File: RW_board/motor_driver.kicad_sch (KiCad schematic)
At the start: 0 parts

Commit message: Started working on motor driver schematic, added libraries, added motor cad
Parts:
- added IC1: MCT8315Z0HRRYR, QFN50P600X400X80-33N-D, symbol RW_Imports:MCT8315Z0HRRYR
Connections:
- new net GND: IC1.10 (PGND_1), IC1.14 (PGND_2)
- new net Motor_12V: IC1.8 (VM_1), IC1.9 (VM_2)
- new net Motor_Brake: IC1.31 (BRAKE)
- new net Motor_DIR: IC1.29 (DIR)
- new net Motor_FGOUT: IC1.1 (FGOUT)
- new net Motor_OUTA: IC1.11 (OUTA)
- new net Motor_OUTB: IC1.12 (OUTB)
- new net Motor_OUTC: IC1.13 (OUTC)
- new net Motor_PWM: IC1.32 (PWM)

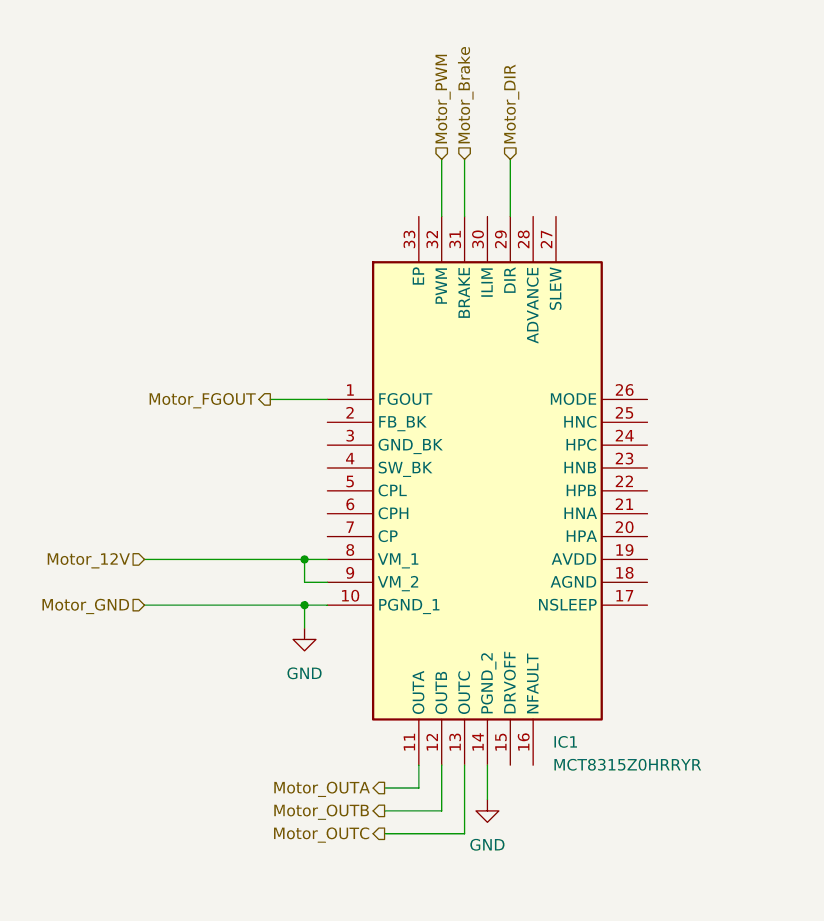
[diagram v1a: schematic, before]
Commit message: Added motor symbol/footprint, worked more on schematic
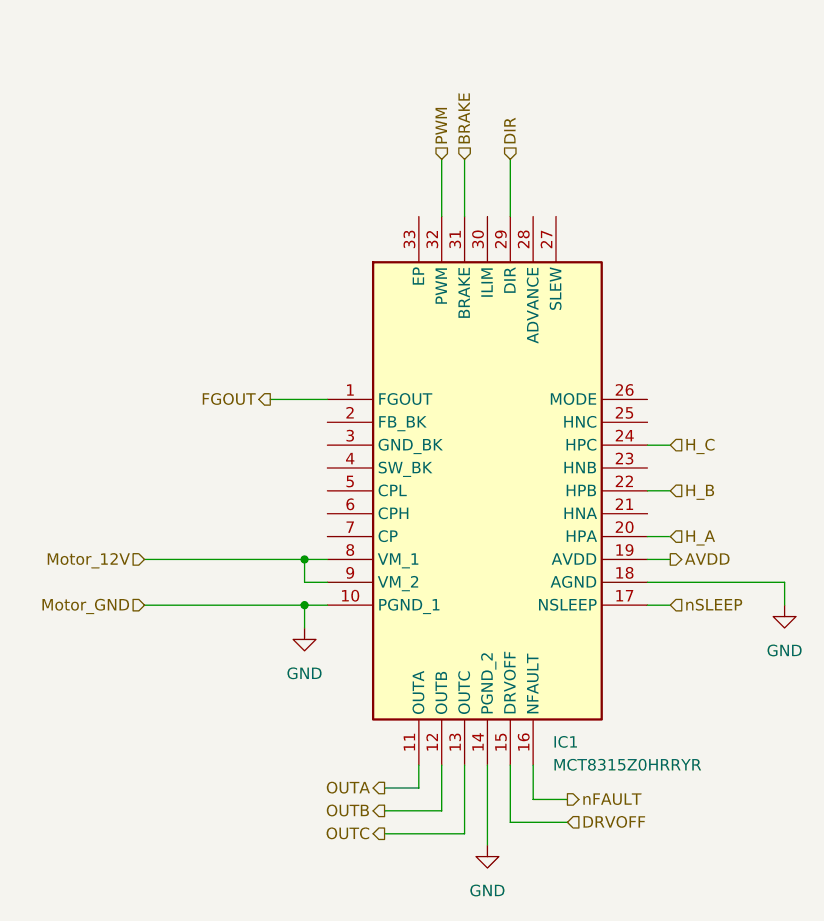
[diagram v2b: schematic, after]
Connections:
- net GND: now also IC1.18 (AGND)
- net DRVOFF: now reaches IC1.15 (DRVOFF)
- net nFAULT: now reaches IC1.16 (NFAULT)
- net nSLEEP: now reaches IC1.17 (NSLEEP)
- net AVDD: now reaches IC1.19 (AVDD)
- net H_A: now reaches IC1.20 (HPA)
- net H_B: now reaches IC1.22 (HPB)
- net H_C: now reaches IC1.24 (HPC)
- net Motor_Brake renamed BRAKE
- net Motor_DIR renamed DIR
- net Motor_FGOUT renamed FGOUT
- net Motor_OUTA renamed OUTA
- net Motor_OUTB renamed OUTB
- net Motor_OUTC renamed OUTC
- net Motor_PWM renamed PWM

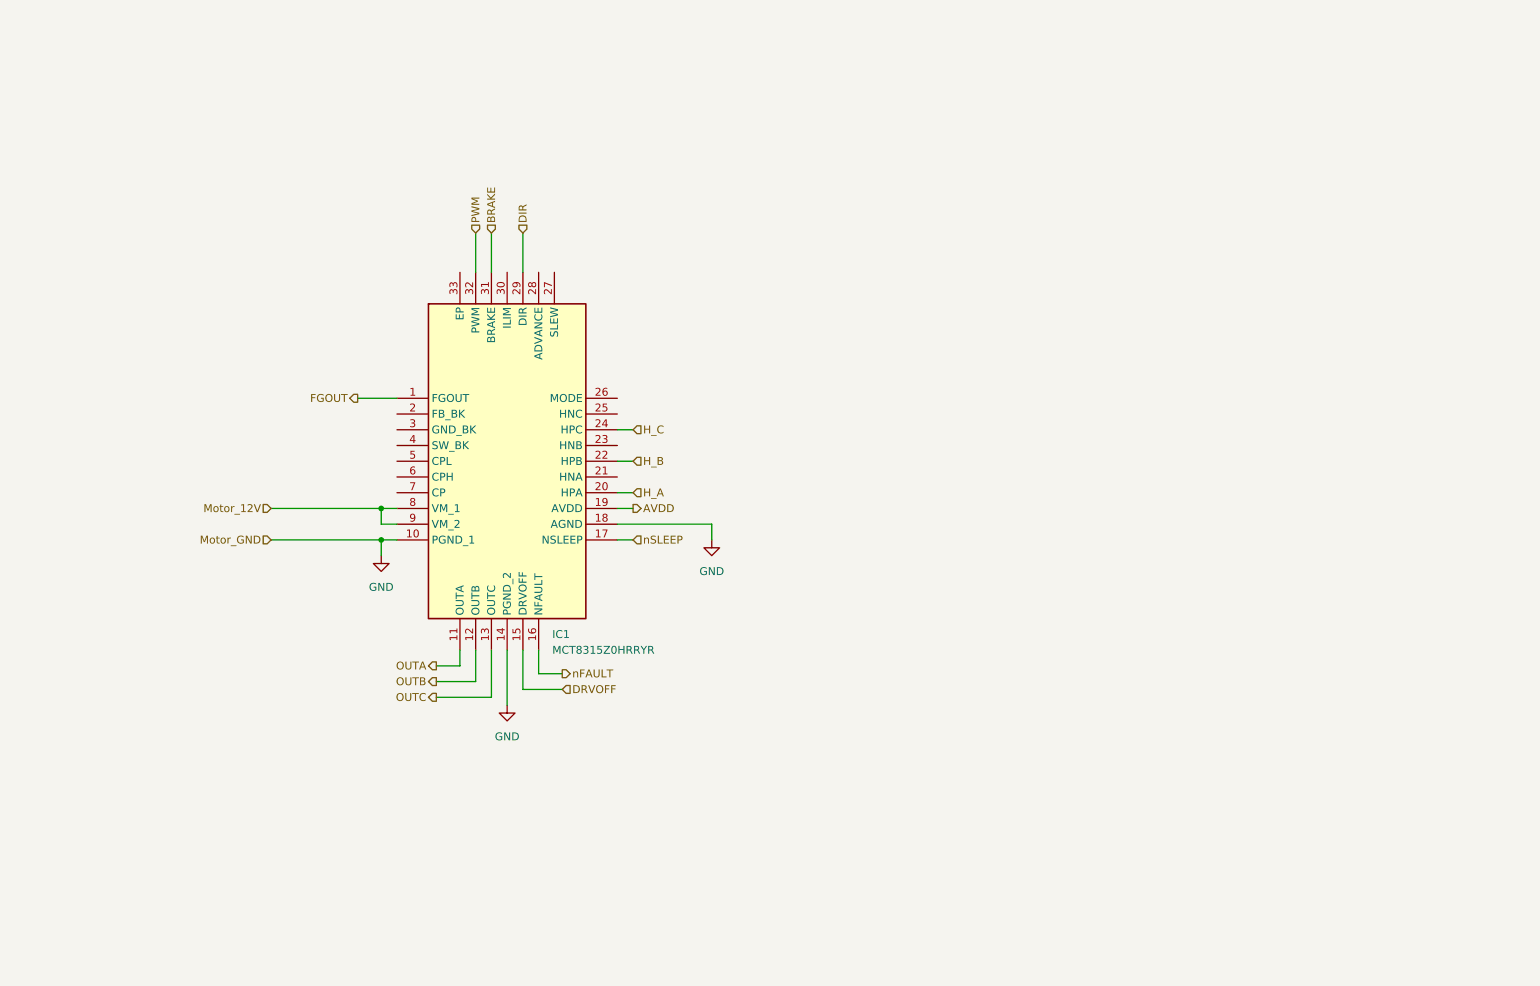
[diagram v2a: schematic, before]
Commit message: Switched to MCT8316, added supporting components
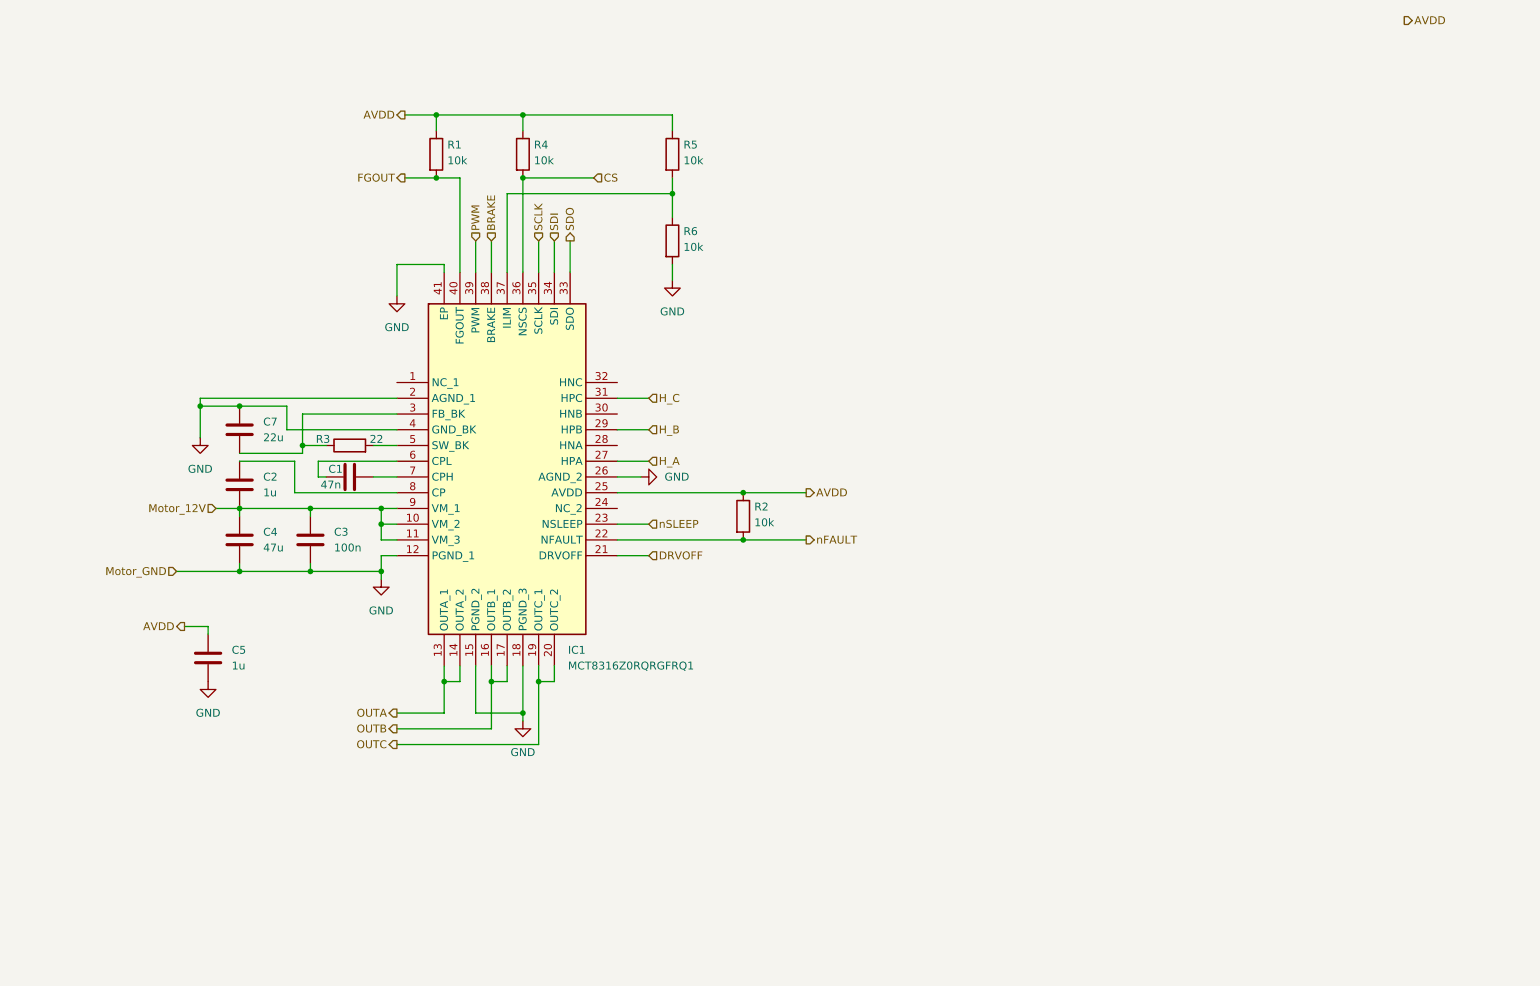
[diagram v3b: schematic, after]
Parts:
- removed IC1: MCT8315Z0HRRYR, QFN50P600X400X80-33N-D, symbol RW_Imports:MCT8315Z0HRRYR
- added C1: 47n, Capacitor_SMD:C_0402_1005Metric, symbol Device:C
- added C2, C5: 1u, Capacitor_SMD:C_0402_1005Metric, symbol Device:C
- added C3: 100n, Capacitor_SMD:C_0402_1005Metric, symbol Device:C
- added C4: 47u, Capacitor_SMD:C_0805_2012Metric, symbol Device:C
- added C7: 22u, Capacitor_SMD:C_0402_1005Metric, symbol Device:C
- added IC1: MCT8316Z0RQRGFRQ1, QFN50P500X700X100-41N-D, symbol RW_Imports:MCT8316Z0RQRGFRQ1
- added R1, R2, R4, R5, R6: 10k, symbol Device:R
- added R3: 22, Capacitor_SMD:C_0402_1005Metric, symbol Device:R
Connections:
- net AVDD: now also C5.1, IC1.25 (AVDD), R1.1, R2.1, R4.1, R5.1
- net BRAKE: now also IC1.38 (BRAKE)
- net DRVOFF: now also IC1.21 (DRVOFF)
- net FGOUT: now also IC1.40 (FGOUT), R1.2
- net GND: now also C3.2, C4.2, C5.2, C7.2, IC1.12 (PGND_1), IC1.15 (PGND_2), IC1.18 (PGND_3), IC1.2 (AGND_1), IC1.26 (AGND_2), IC1.4 (GND_BK), IC1.41 (EP), R6.2
- net H_A: now also IC1.27 (HPA)
- net H_B: now also IC1.29 (HPB)
- net H_C: now also IC1.31 (HPC)
- net Motor_12V: now also C2.2, C3.1, C4.1, IC1.10 (VM_2), IC1.11 (VM_3), IC1.9 (VM_1)
- net OUTA: now also IC1.13 (OUTA_1), IC1.14 (OUTA_2)
- net OUTB: now also IC1.16 (OUTB_1), IC1.17 (OUTB_2)
- net OUTC: now also IC1.19 (OUTC_1), IC1.20 (OUTC_2)
- net PWM: now also IC1.39 (PWM)
- net nFAULT: now also IC1.22 (NFAULT), R2.2
- net nSLEEP: now also IC1.23 (NSLEEP)
- new net: C2.1, IC1.8 (CP)
- new net: IC1.37 (ILIM), R5.2, R6.1
- new net: C7.1, IC1.3 (FB_BK), R3.1
- new net: IC1.5 (SW_BK), R3.2
- new net: C1.1, IC1.6 (CPL)
- new net: C1.2, IC1.7 (CPH)
- new net CS: IC1.36 (NSCS), R4.2
- new net SCLK: IC1.35 (SCLK)
- new net SDI: IC1.34 (SDI)
- new net SDO: IC1.33 (SDO)

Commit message: Completed motor driver schematic
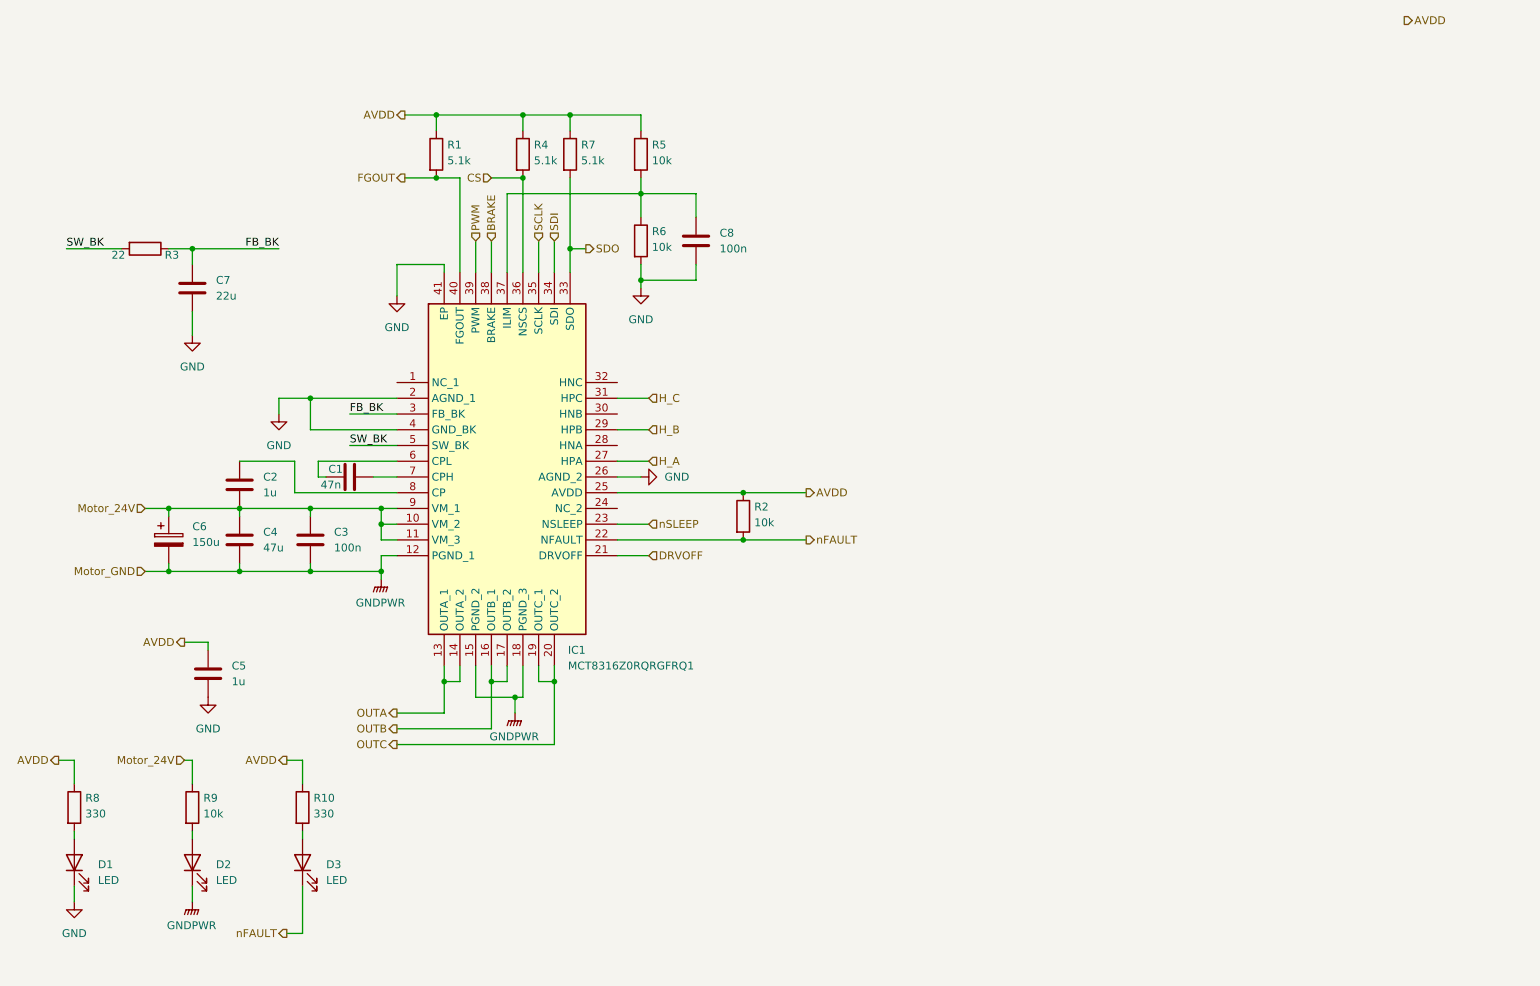
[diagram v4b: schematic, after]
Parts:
- added C6: 150u, Capacitor_SMD:CP_Elec_6.3x7.7, symbol Device:C_Polarized
- added C8: 100n, Capacitor_SMD:C_0402_1005Metric, symbol Device:C
- added D1, D2, D3: LED, symbol Device:LED
- added R10, R8: 330, symbol Device:R
- added R7: 5.1k, symbol Device:R
- added R9: 10k, symbol Device:R
- R1, R4: value 10k -> 5.1k
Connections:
- net AVDD: now also R10.1, R7.1, R8.1
- net GND: now also C8.2, D1.1 (K); no longer C3.2, C4.2, IC1.12 (PGND_1), IC1.15 (PGND_2), IC1.18 (PGND_3)
- net SDO: now also R7.2
- net nFAULT: now also D3.1 (K)
- net at IC1.37 (ILIM), R5.2, R6.1: now also C8.1
- net FB_BK: now reaches C7.1, IC1.3 (FB_BK), R3.1
- net SW_BK: now reaches IC1.5 (SW_BK), R3.2
- net Motor_12V renamed Motor_24V
- net Motor_24V: now also C6.1, R9.1
- new net: D1.2 (A), R8.2
- new net: D2.2 (A), R9.2
- new net: D3.2 (A), R10.2
- new net GNDPWR: C3.2, C4.2, C6.2, D2.1 (K), IC1.12 (PGND_1), IC1.15 (PGND_2), IC1.18 (PGND_3)
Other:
- moved on the sheet: C5, R5, R6

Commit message: Completed MCU schematic, connected with driver schematic
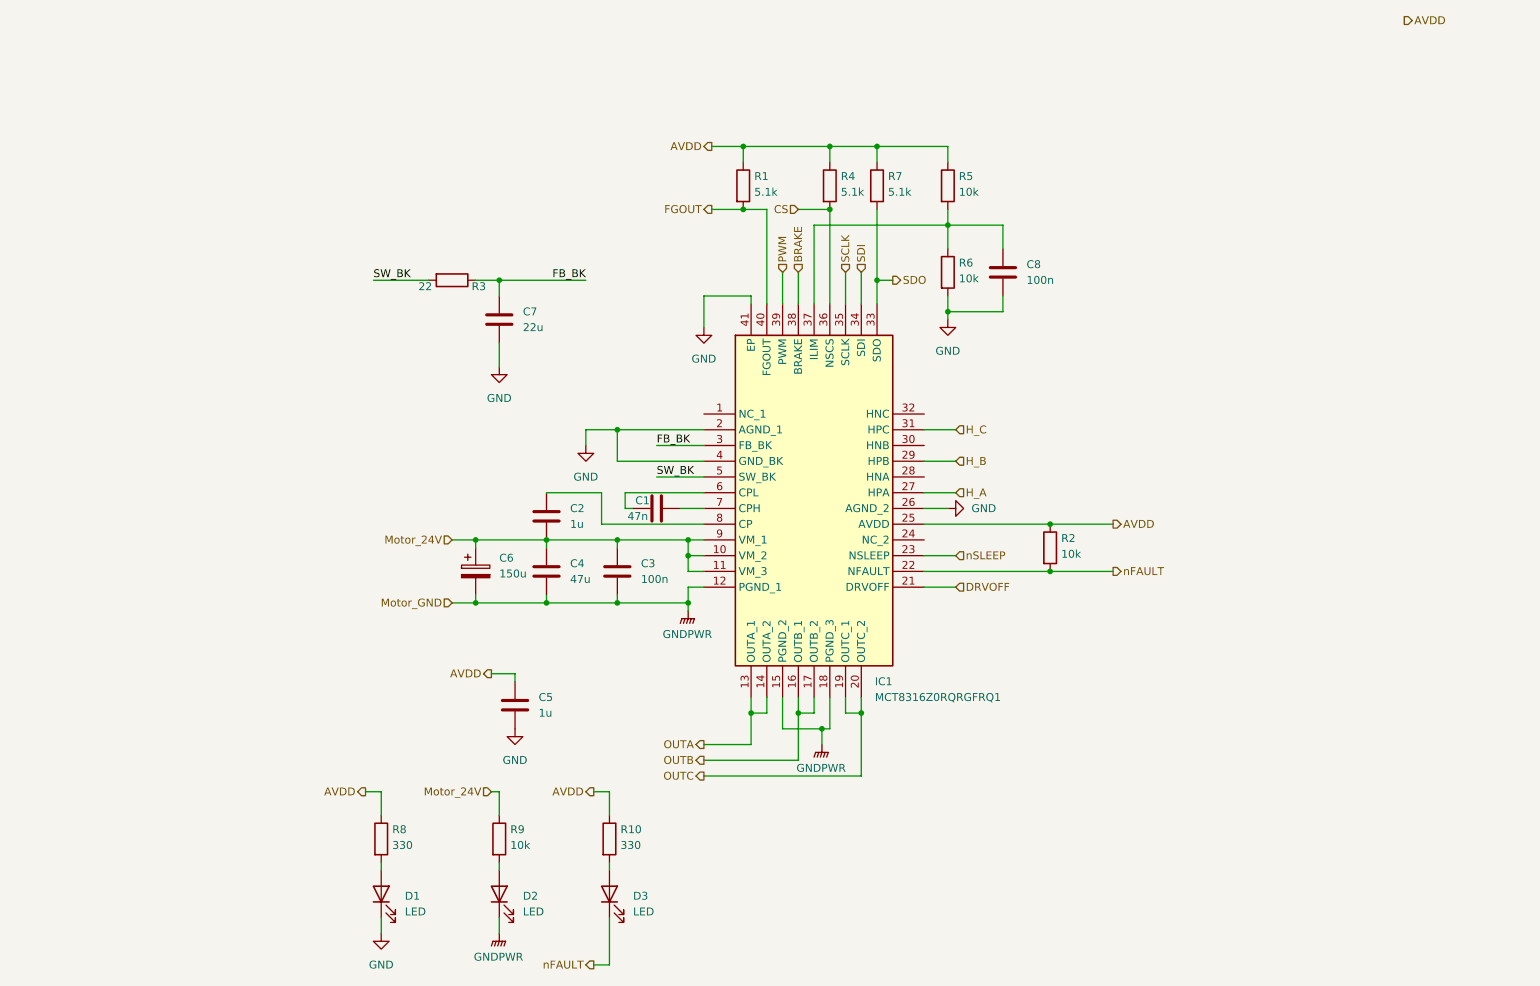
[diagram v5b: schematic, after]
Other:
- moved on the sheet: C1, C2, C3, C4, C5, C6, C7, C8, D1, D2, D3, IC1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
